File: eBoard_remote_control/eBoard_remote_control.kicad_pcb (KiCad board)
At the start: 2 copper layers, 34 x 99.9 mm, 38 parts, among them J1 SWDIO_conn, P1 USB, U1 MDBT42, U2 AP2112(3.3V), U3 MCP73831T-2ACI/OT, U4 CP2104, U5 AH49ENTR-G1, U6 AH49ENTR-G1, U7 AH49ENTR-G1, X2 JSTPH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

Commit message: V2 update
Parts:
- added C9: 0.1uF, eBoard_remote_control:C0603, F.Cu at (193.0, 143.3)
- added D4: 1n4148, Adafruit nRF52 Bluefruit Feather rev G:SOD-323, F.Cu at (202.3, 145.2)
- added R2: 10K, eBoard_remote_control:0603-NO, F.Cu at (200.5, 145.2)
- added SJ2: BAT, Adafruit nRF52 Bluefruit Feather rev G:SOLDERJUMPER_CLOSEDWIRE, B.Cu at (196.8, 145.0)
- C1, C10, C12, C2, C4: footprint eBoard_remote_control:0603-NO -> eBoard_remote_control:C0603
- C3, C5, C6, C7, C8: footprint eBoard_remote_control:0805-NO -> eBoard_remote_control:C0603
- J1: footprint Connector_PinHeader_2.54mm:PinHeader_1x05_P2.54mm_Vertical -> Connector_PinHeader_1.27mm:PinHeader_2x05_P1.27mm_Vertical_SMD
- moved J1 24.0 mm to (207.0, 143.1), turned to 90 degrees
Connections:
- J1 pad 1: GND -> 3.3V
- J1 pad 2: 3.3V -> /SWDIO
- J1 pad 3: /SWDIO -> GND
- J1 pad 5: /RESET -> GND
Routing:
- net /RESET: track 9.68 -> 37.4 mm, vias 0 -> 3
- net /SWDIO: track 6.45 -> 25.7 mm, vias 0 -> 2
- net /SWCLK: track 7.84 -> 23.8 mm, vias 0 -> 2
- net Net-(C9-Pad1): track 0.00 -> 4.01 mm, vias 0 -> 1
- net /DTR: track 0.00 -> 3.79 mm
- net 3.3V: track 136.8 -> 140.4 mm, vias 2 -> 3
- net GND: track 27.8 -> 31.2 mm, vias 96 -> 106
- net VBAT: track 76.3 -> 77.4 mm

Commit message: V2.1
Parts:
- SJ2: moved to F.Cu
- moved C9 4.13 mm to (192.7, 147.4)
- moved S2 3.51 mm to (194.7, 154.9)
- moved SJ2 2.37 mm to (197.3, 147.3)
- moved C21 1.28 mm to (198.1, 66.3)
- moved C14 1.22 mm to (199.9, 66.3)
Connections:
- J1 pad 6: Net-(J1-Pad6) -> /SWO
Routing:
- net /SWO: track 0.00 -> 18.9 mm
- net /VBB: track 49.9 -> 53.4 mm
- net /DTR: track 3.79 -> 7.08 mm, vias 0 -> 2
- net VBAT: track 77.4 -> 74.7 mm
- net Net-(C9-Pad1): track 4.01 -> 3.10 mm, vias 1 -> 0
- net /RESET: track 37.4 -> 37.1 mm, vias 3 -> 2
- net GND: vias 106 -> 100
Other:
- board text added: "1"
- board text added: "OFF"
- board text added: "ON"

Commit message: this
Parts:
- removed DIS1: OLED, eBoard_remote_control:OLED
- added Ue: SSD1306, eBoard_remote_control:SSD1306_OLED-0.91-128x32, B.Cu at (178.2, 86.0)
- moved C6 16.8 mm to (190.4, 111.6)
- moved C8 16.8 mm to (196.6, 112.4)
- moved U2 16.8 mm to (193.5, 112.3)
- moved R5 16.8 mm to (191.1, 114.3)
- moved R9 15.5 mm to (191.2, 142.8)
- moved R3 15.3 mm to (179.1, 120.3), turned to 90 degrees
- moved C1 15.3 mm to (190.1, 123.4), turned to 180 degrees
- moved C2 12.2 mm to (190.1, 129.2), turned to 180 degrees
- moved C5 11.6 mm to (181.5, 120.8), turned to 0 degrees
- moved CHG1 11.6 mm to (179.1, 124.0)
- moved R4 11.3 mm to (203.6, 120.3), turned to 270 degrees
- moved X4 11.1 mm to (190.0, 126.3), turned to 90 degrees
- moved C4 9.88 mm to (197.8, 119.4), turned to 180 degrees
- moved R6 9.87 mm to (201.9, 120.4), turned to 90 degrees
- moved C12 8.95 mm to (200.3, 120.4), turned to 90 degrees
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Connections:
- J1 pad 8: Net-(J1-Pad8) -> (no net)
- P1 pad 4: Net-(P1-Pad4) -> (no net)
- S1 pad P3: Net-(S1-PadP3) -> (no net)
- S2 pad 3: Net-(S2-Pad3) -> (no net)
- U1 pad 18: /A3 -> (no net)
- U1 pad 22: Net-(U1-Pad22) -> (no net)
- U1 pad 23: Net-(U1-Pad23) -> (no net)
- U1 pad 25: /P0.11 -> (no net)
- U1 pad 26: /SCK -> (no net)
- U1 pad 27: /MOSI -> (no net)
- U1 pad 28: /MISO -> (no net)
- U1 pad 29: /P0.15 -> (no net)
- U1 pad 30: /P0.16 -> (no net)
- U1 pad 31: Net-(U1-Pad31) -> (no net)
- U1 pad 33: Net-(U1-Pad33) -> (no net)
- U1 pad 34: /DFU -> (no net)
- U1 pad 38: /FRST -> (no net)
- U1 pad 4: /P0.27 -> (no net)
- U1 pad 40: Net-(U1-Pad40) -> (no net)
- U1 pad 41: Net-(U1-Pad41) -> (no net)
- U1 pad 5: /A4/0.28 -> (no net)
- U1 pad 6: /A5/0.29 -> (no net)
- U1 pad 7: /A6/P0.30 -> (no net)
- U2 pad 4: Net-(U2-Pad4) -> (no net)
- U4 pad 1: Net-(U4-Pad1) -> (no net)
- U4 pad 10: Net-(U4-Pad10) -> (no net)
- U4 pad 11: Net-(U4-Pad11) -> (no net)
- U4 pad 12: Net-(U4-Pad12) -> (no net)
- U4 pad 13: Net-(U4-Pad13) -> (no net)
- U4 pad 14: Net-(U4-Pad14) -> (no net)
- U4 pad 15: Net-(U4-Pad15) -> (no net)
- U4 pad 17: Net-(U4-Pad17) -> (no net)
- U4 pad 18: Net-(U4-Pad18) -> (no net)
- U4 pad 19: Net-(U4-Pad19) -> (no net)
- U4 pad 22: Net-(U4-Pad22) -> (no net)
- U4 pad 24: Net-(U4-Pad24) -> (no net)
- U4 pad 9: Net-(U4-Pad9) -> (no net)
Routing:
- net VBAT: track 74.7 -> 1.86 mm, vias 1 -> 0
- net /A1: track 76.1 -> 15.8 mm, vias 2 -> 1
- net 3.3V: track 140.7 -> 84.7 mm, vias 3 -> 1
- net /VBB: track 53.4 -> 0.37 mm, vias 1 -> 0
- net /A2: track 81.1 -> 36.5 mm, vias 2 -> 1
- net /P0.07: track 48.8 -> 7.18 mm, vias 2 -> 1
- net /RESET: track 37.1 -> 0.00 mm, vias 2 -> 0
- net /TXD: track 29.1 -> 0.00 mm, vias 2 -> 0
- net /SWDIO: track 25.7 -> 0.00 mm, vias 2 -> 0
- net /SWCLK: track 23.8 -> 0.00 mm, vias 2 -> 0
- net /A0: track 72.3 -> 50.6 mm, vias 2 -> 1
- net Net-(R9-Pad1): track 19.8 -> 0.00 mm
- net GND: track 31.2 -> 12.0 mm, vias 100 -> 38
- net /SWO: track 18.9 -> 0.00 mm
- net /SDA: track 13.6 -> 0.00 mm
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
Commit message: this
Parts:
- added R1: 1K, eBoard_remote_control:0603-NO, F.Cu at (192.8, 149.3)
- moved R9 6.32 mm to (191.8, 136.4)
- renumbered Ue to U8
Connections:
- U1 pad 2: /SDA -> (no net)
- U1 pad 3: /SCL -> (no net)
- U8 pad 1: Net-(U8-Pad1) -> (no net)
- U8 pad 10: Net-(U8-Pad10) -> (no net)
- U8 pad 11: Net-(U8-Pad11) -> (no net)
- U8 pad 12: Net-(U8-Pad12) -> (no net)
- U8 pad 13: Net-(U8-Pad13) -> (no net)
- U8 pad 14: Net-(U8-Pad14) -> (no net)
- U8 pad 2: Net-(U8-Pad2) -> (no net)
- U8 pad 3: Net-(U8-Pad3) -> (no net)
- U8 pad 4: Net-(U8-Pad4) -> (no net)
- U8 pad 5: Net-(U8-Pad5) -> (no net)
- U8 pad 6: Net-(U8-Pad6) -> (no net)
- U8 pad 7: Net-(U8-Pad7) -> (no net)
- U8 pad 8: Net-(U8-Pad8) -> (no net)
- U8 pad 9: Net-(U8-Pad9) -> (no net)
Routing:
- net GND: vias 38 -> 36

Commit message: this
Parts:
- removed P1: USB, eBoard_remote_control:USB-MICRO-B
- added C11: 10µF, eBoard_remote_control:C0603, F.Cu at (181.2, 70.1)
- added C13: 100n, eBoard_remote_control:C0603, F.Cu at (182.9, 69.9)
- added J2: 105450-0101, eBoard_remote_control:105450-0101, F.Cu at (184.7, 137.4)
- added X1: JSTPH, eBoard_remote_control:JSTPH2, F.Cu at (171.3, 104.2)
- moved C6 28.3 mm to (162.1, 112.2)
- moved C8 28.3 mm to (168.3, 113.1)
- moved U2 28.3 mm to (165.2, 112.9)
- moved R5 28.3 mm to (162.8, 115.0)
- moved C2 25.5 mm to (190.9, 103.7)
- moved X4 25.5 mm to (190.9, 100.8)
- moved C1 25.5 mm to (190.9, 97.9)
- moved C9 6.42 mm to (198.1, 150.8)
- moved C10 6.01 mm to (190.4, 141.4)
- moved D4 5.99 mm to (196.3, 145.7)
- moved R2 5.99 mm to (194.5, 145.6)
- moved C12 5.66 mm to (201.5, 114.8)
- moved C3 5.66 mm to (196.1, 117.6)
- moved C4 5.66 mm to (198.9, 113.9)
- moved L2 5.66 mm to (198.9, 115.4)
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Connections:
- U4 pad 3: /USBD+ -> USBD+
- U4 pad 4: /USBD- -> USBD-
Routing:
- net /A0: track 50.6 -> 0.00 mm, vias 1 -> 0
- net 3.3V: track 84.7 -> 44.5 mm, vias 1 -> 0
- net VBUS: track 8.53 -> 0.00 mm
- net /USBD-: track 8.02 -> 0.00 mm, vias 2 -> 0
- net /USBD+: track 8.01 -> 0.00 mm, vias 2 -> 0
- net GND: track 12.0 -> 6.32 mm, vias 36 -> 18
- net Net-(C7-Pad1): track 2.05 -> 0.00 mm
- net (no net): track 0.00 -> 1.01 mm
- removed copper zone on B.Cu, net GND
- removed copper zone on F.Cu, net GND
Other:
- outline, holes or cut-outs redrawn

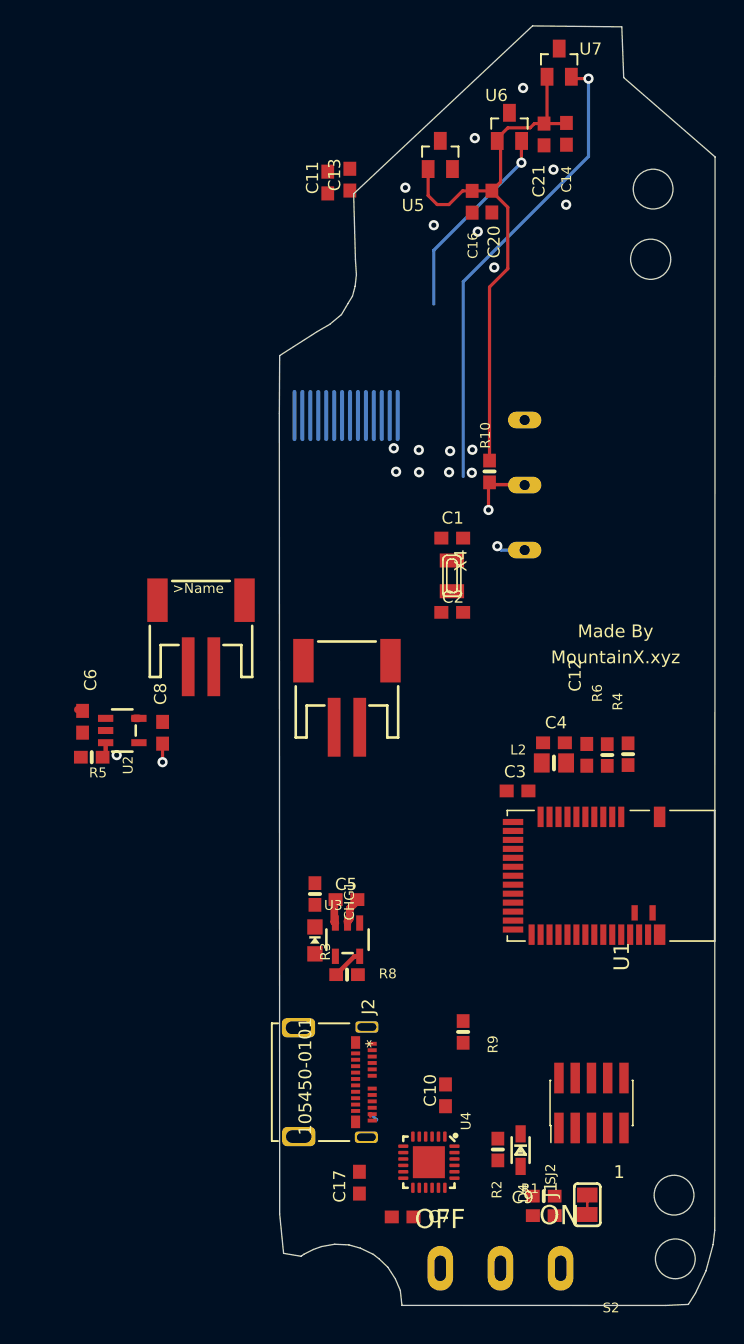
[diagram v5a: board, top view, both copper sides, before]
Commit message: added dual jst and 3d models
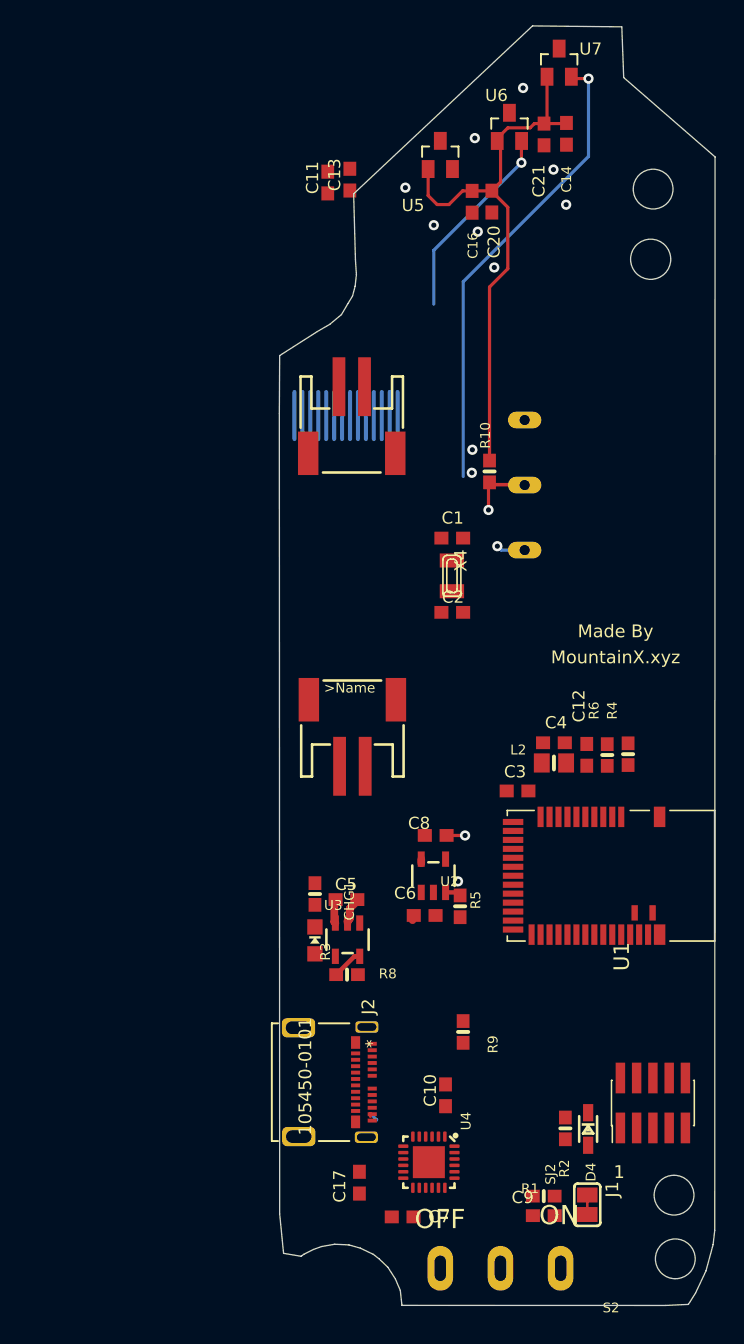
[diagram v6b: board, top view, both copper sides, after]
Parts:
- moved R5 31.0 mm to (191.6, 126.6), turned to 270 degrees
- moved C6 30.7 mm to (188.8, 127.4), turned to 0 degrees
- moved U2 26.8 mm to (189.5, 124.2), turned to 0 degrees
- moved C8 22.8 mm to (189.7, 121.1), turned to 0 degrees
- moved X2 19.2 mm to (183.1, 89.8), turned to 180 degrees
- moved X1 14.2 mm to (183.2, 112.0)
- moved D4 5.53 mm to (201.6, 144.0)
- moved R2 5.53 mm to (199.8, 144.0)
- moved J1 4.80 mm to (206.6, 142.0)
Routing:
- net GND: vias 18 -> 13
- net Net-(U8-Pad2): vias 1 -> 0

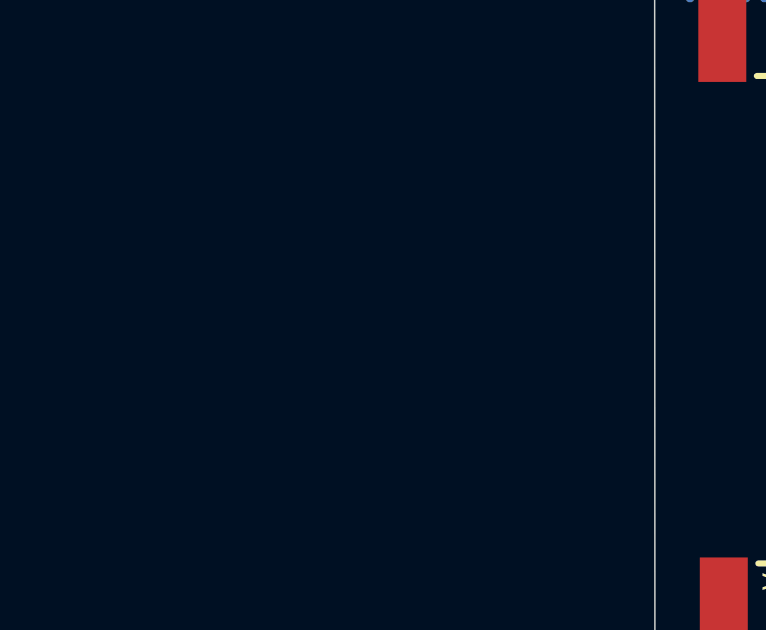
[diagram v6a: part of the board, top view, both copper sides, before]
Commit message: oled schem
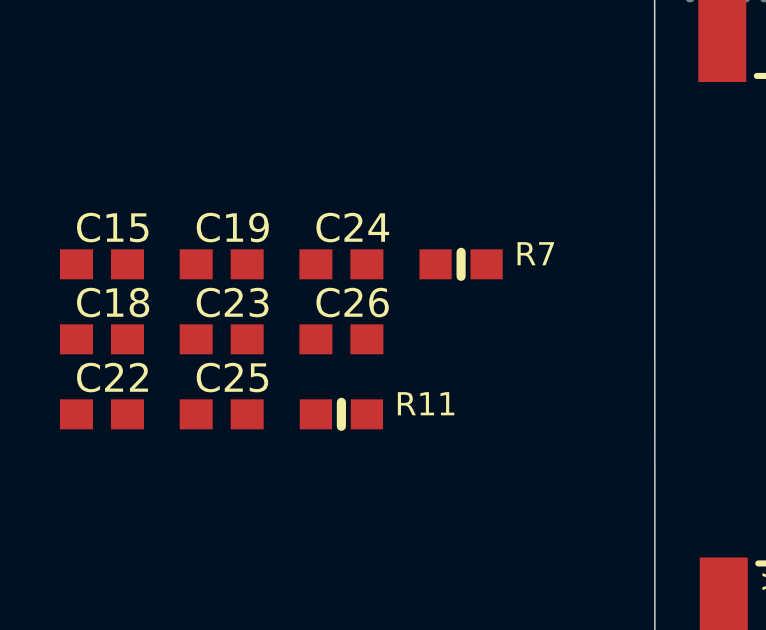
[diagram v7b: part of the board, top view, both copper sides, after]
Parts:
- added C15: 100nF, eBoard_remote_control:C0603, F.Cu at (159.0, 99.0)
- added C18: 1uF, eBoard_remote_control:C0603, F.Cu at (159.0, 101.5)
- added C19: 1uF, eBoard_remote_control:C0603, F.Cu at (163.0, 99.0)
- added C22: 1uF, eBoard_remote_control:C0603, F.Cu at (159.0, 104.0)
- added C23: 10uF, eBoard_remote_control:C0603, F.Cu at (163.0, 101.5)
- added C24: 10uF, eBoard_remote_control:C0603, F.Cu at (167.0, 99.0)
- added C25: 1uF, eBoard_remote_control:C0603, F.Cu at (163.0, 104.0)
- added C26: 1uF, eBoard_remote_control:C0603, F.Cu at (167.0, 101.5)
- added R11: 390k, eBoard_remote_control:0603-NO, F.Cu at (167.0, 104.0)
- added R7: 10K, eBoard_remote_control:0603-NO, F.Cu at (171.0, 99.0)
- C13, C16, C21: value 100n -> 100nF
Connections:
- U1 pad 2: (no net) -> SDA
- U1 pad 3: (no net) -> SCL
- U8 pad 10: (no net) -> SCL
- U8 pad 11: (no net) -> SDA
- U8 pad 5: (no net) -> 3V3
- U8 pad 7: (no net) -> GND
- U8 pad 8: (no net) -> 3V3

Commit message: started Layout V3
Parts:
- removed C25, C26: 1uF, eBoard_remote_control:C0603
- removed R10: 1K, eBoard_remote_control:0603-NO
- moved C18 38.8 mm to (192.8, 82.2), turned to 90 degrees
- moved C22 36.2 mm to (188.0, 82.2), turned to 270 degrees
- moved C19 32.4 mm to (190.8, 82.2), turned to 90 degrees
- moved C15 31.4 mm to (189.8, 92.5), turned to 180 degrees
- moved R11 27.9 mm to (184.5, 82.2), turned to 90 degrees
- moved C23 24.8 mm to (181.2, 84.8), turned to 180 degrees
- moved R7 22.7 mm to (186.2, 82.2), turned to 90 degrees
- moved C24 21.4 mm to (181.2, 83.0), turned to 180 degrees
- moved C1 15.4 mm to (201.3, 109.3), turned to 0 degrees
- moved X2 12.3 mm to (182.5, 102.0), turned to 0 degrees
- moved C8 11.0 mm to (187.3, 131.8), turned to 270 degrees
- moved C2 10.9 mm to (201.3, 106.9), turned to 0 degrees
- moved X4 10.5 mm to (198.4, 108.1), turned to 270 degrees
- moved U2 8.14 mm to (190.0, 132.4)
- moved R5 8.14 mm to (192.1, 134.8)
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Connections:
- C11 pad 1: Net-(C11-Pad1) -> 3V3
- C13 pad 1: Net-(C11-Pad1) -> 3V3
- U6 pad 1: 3.3V -> 3V3
- U8 pad 1: (no net) -> Net-(C18-Pad1)
- U8 pad 12: (no net) -> Net-(R11-Pad1)
- U8 pad 13: (no net) -> Net-(C23-Pad2)
- U8 pad 14: (no net) -> Net-(C24-Pad2)
- U8 pad 2: (no net) -> Net-(C18-Pad2)
- U8 pad 3: (no net) -> Net-(C19-Pad1)
- U8 pad 4: (no net) -> Net-(C19-Pad2)
- U8 pad 6: (no net) -> Net-(C22-Pad2)
- U8 pad 9: (no net) -> Net-(R7-Pad1)
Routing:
- net 3.3V: track 44.5 -> 0.33 mm
- net SCL: track 0.00 -> 40.5 mm, vias 0 -> 1
- net SDA: track 0.00 -> 40.5 mm, vias 0 -> 1
- net VBAT: track 1.86 -> 39.5 mm, vias 0 -> 1
- net /A2: track 36.5 -> 1.86 mm
- net /RESET: track 0.00 -> 29.3 mm
- net VBUS: track 0.00 -> 25.6 mm
- net Net-(C2-Pad1): track 0.00 -> 17.3 mm
- net /VBB: track 0.37 -> 17.4 mm
- net Net-(C1-Pad1): track 0.00 -> 14.9 mm
- net /SWO: track 0.00 -> 14.5 mm, vias 0 -> 2
- net /SWDIO: track 0.00 -> 14.3 mm, vias 0 -> 2
- net /SWCLK: track 0.00 -> 13.9 mm, vias 0 -> 2
- net Net-(C18-Pad2): track 0.00 -> 12.7 mm, vias 0 -> 1
- net /A1: track 15.8 -> 3.86 mm
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- added copper zone on F.Cu, net VBAT
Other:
- net class Power added: clearance 0.2, trace_width 0.35, via_dia 0.8, via_drill 0.4
- net class smaller added: clearance 0.2, trace_width 0.2, via_dia 0.5, via_drill 0.3
